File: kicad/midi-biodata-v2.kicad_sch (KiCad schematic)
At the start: 32 parts, among them J1 DIN-5_180degree, J2 PJ-320B, J3 Conn_01x14_Pin, J5 PJ-320B, J6 PJ-320B, U1 SN74LVC1G07DBVR, U3 LMC555xM

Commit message: send to jlcpcb
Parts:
- C5: value 1uF -> 100uF
- D8, D9: LCSC C85401 -> C294611
- J3: footprint Connector_PinHeader_2.54mm:PinHeader_1x12_P2.54mm_Vertical -> Connector_PinHeader_2.54mm:PinHeader_1x13_P2.54mm_Vertical
- RV1: footprint Potentiometer_THT:Potentiometer_Bourns_3296W_Vertical -> Potentiometer_THT:Potentiometer_Alps_RK09K_Single_Vertical
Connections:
- net +3V3 is gone; now on net +5V: J3.12 (Pin_12)
- net GND: now also J3.13 (Pin_13)
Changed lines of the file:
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@@
 			)
 		)
-		(property "Value" "1uF"
+		(property "Value" "100uF"
 			(at 141.224 40.386 0)
 			(effects
@@
 			)
 		)
-		(property "LCSC" "C85401"
+		(property "LCSC" "C294611"
 			(at 157.48 60.96 0)
 			(effects
@@
 			)
 		)
-		(property "LCSC" "C85401"
+		(property "LCSC" "C294611"
 			(at 168.91 40.64 0)
 			(effects
@@
 		)
 		(property "Value" "+5V"
-			(at 136.398 163.83 0)
+			(at 135.636 163.83 0)
 			(effects
 				(font
@@
 			)
 		)
-		(property "Footprint" "Connector_PinHeader_2.54mm:PinHeader_1x12_P2.54mm_Vertical"
+		(property "Footprint" "Connector_PinHeader_2.54mm:PinHeader_1x13_P2.54mm_Vertical"
 			(at 124.46 153.67 0)
 			(effects
@@
 			)
 		)
-		(property "Value" "+3V3"
-			(at 133.604 166.878 0)
+		(property "Value" "+5V"
+			(at 135.382 166.624 0)
 			(effects
 				(font
@@
 			)
 		)
-		(property "Footprint" "Potentiometer_THT:Potentiometer_Bourns_3296W_Vertical"
+		(property "Footprint" "Potentiometer_THT:Potentiometer_Alps_RK09K_Single_Vertical"
 			(at 137.16 101.6 0)
 			(effects
@@
 			)
 		)
+		(property "LCSC" ""
+			(at 137.16 101.6 0)
+			(effects
+				(font
+					(size 1.27 1.27)
+				)
+				(hide yes)
+			)
+		)
 		(pin "2"
 		)
@@
 					(unit 1)
 				)
+			)
+		)
+	)
+	(symbol
+		(lib_id "midi-biodata-v2-rescue:GND")
+		(at 129.54 168.91 90)
+		(unit 1)
+		(exclude_from_sim no)
+		(in_bom yes)
+		(on_board yes)
+		(dnp no)
+		(property "Reference" "#PWR018"
+			(at 135.89 168.91 0)
+			(effects
+				(font
+					(size 1.27 1.27)
+				)
+				(hide yes)
+			)
+		)
+		(property "Value" "GND"
+			(at 133.35 168.91 0)
+			(effects
+				(font
+					(size 1.27 1.27)
+				)
+			)
+		)
+		(property "Footprint" ""
+			(at 129.54 168.91 0)
+			(effects
+				(font
+					(size 1.27 1.27)
+				)
+				(hide yes)
+			)
+		)
+		(property "Datasheet" ""
+			(at 129.54 168.91 0)
+			(effects
+				(font
+					(size 1.27 1.27)
+				)
+				(hide yes)
+			)
+		)
+		(property "Description" ""
+			(at 129.54 168.91 0)
+			(effects
+				(font
+					(size 1.27 1.27)
+				)
+				(hide yes)
+			)
+		)
+		(pin "1"
+		)
+		(instances
+			(project "midi-biodata-v2"
+				(path "/0696d548-26ae-48fa-b73e-c6b82482150e"
+					(reference "#PWR018")
+					(unit 1)
+				)

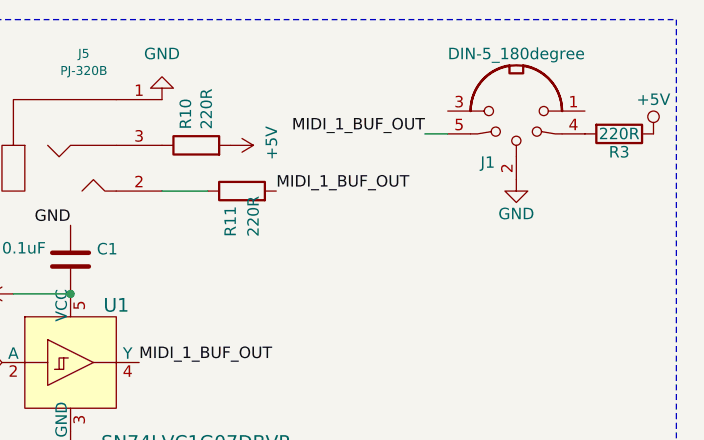
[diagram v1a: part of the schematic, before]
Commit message: fixed midi routing on the pcb board
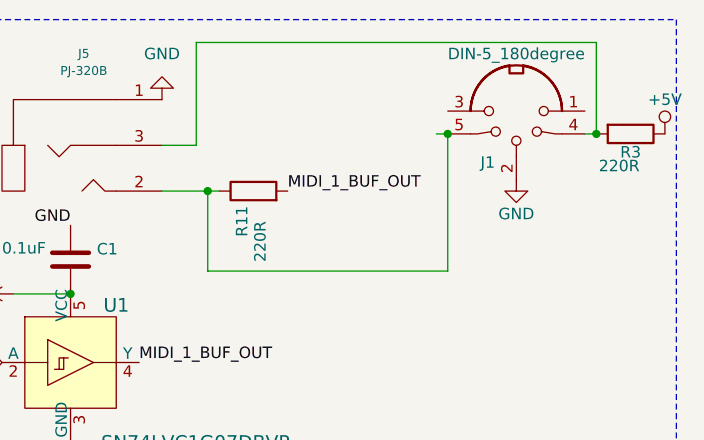
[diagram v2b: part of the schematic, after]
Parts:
- removed R10: 220R, Resistor_SMD:R_0402_1005Metric, symbol Device:R
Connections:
- net MIDI_1_BUF_OUT: no longer J1.5
- net at J1.4, R3.2: now also J5.3
- net at J5.2, R11.1: now also J1.5
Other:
- moved on the sheet: R11, R3

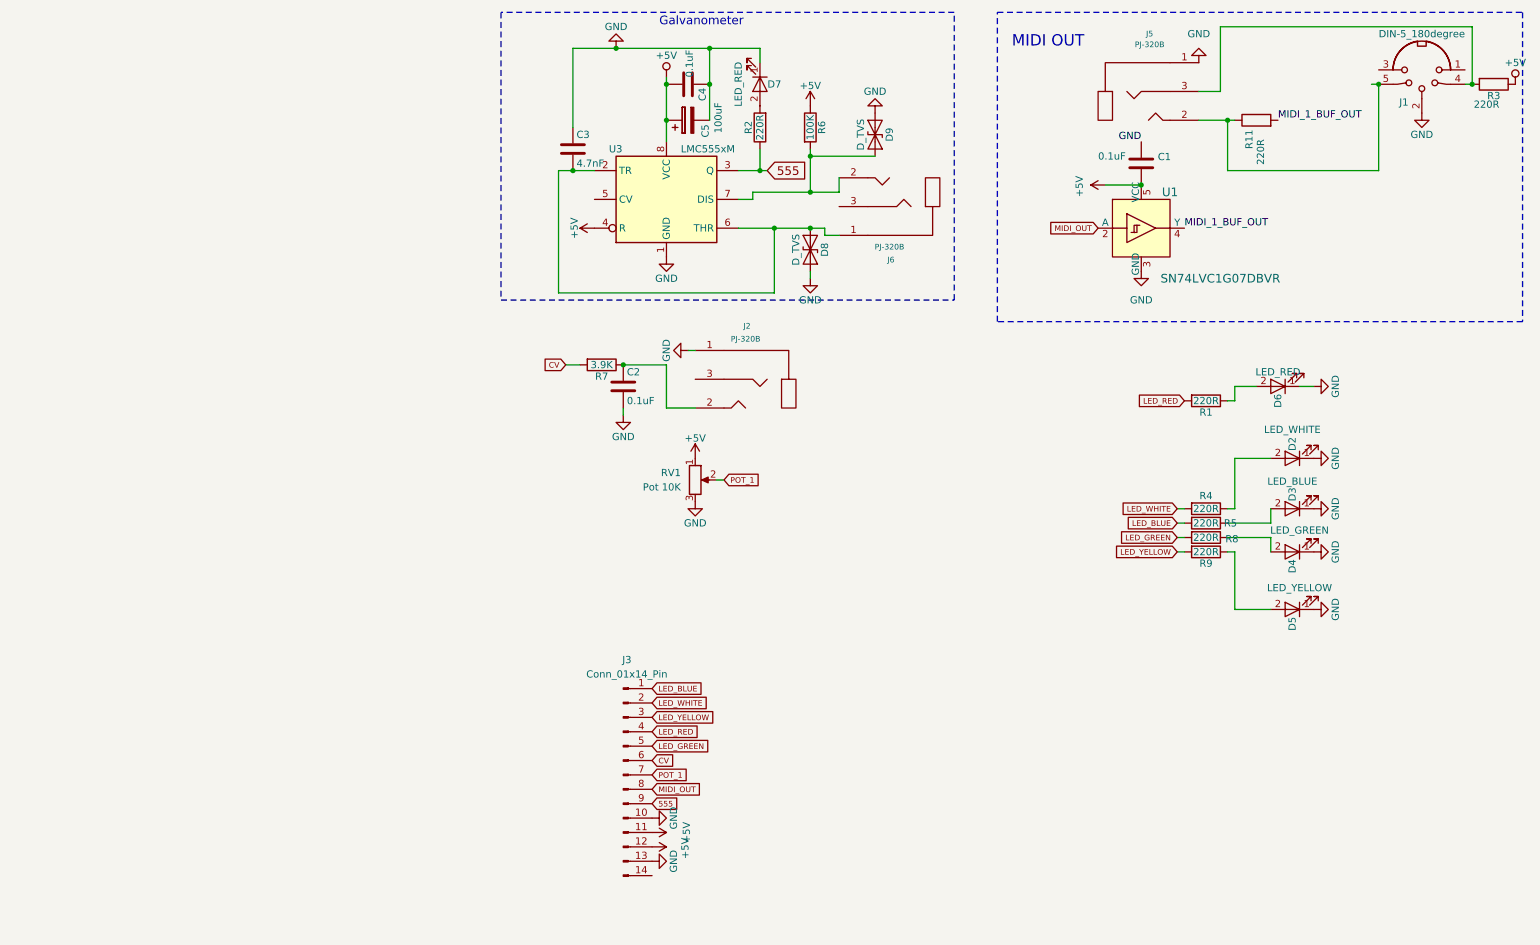
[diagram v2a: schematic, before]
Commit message: cleanup, changed footprint for 3.5mm jack
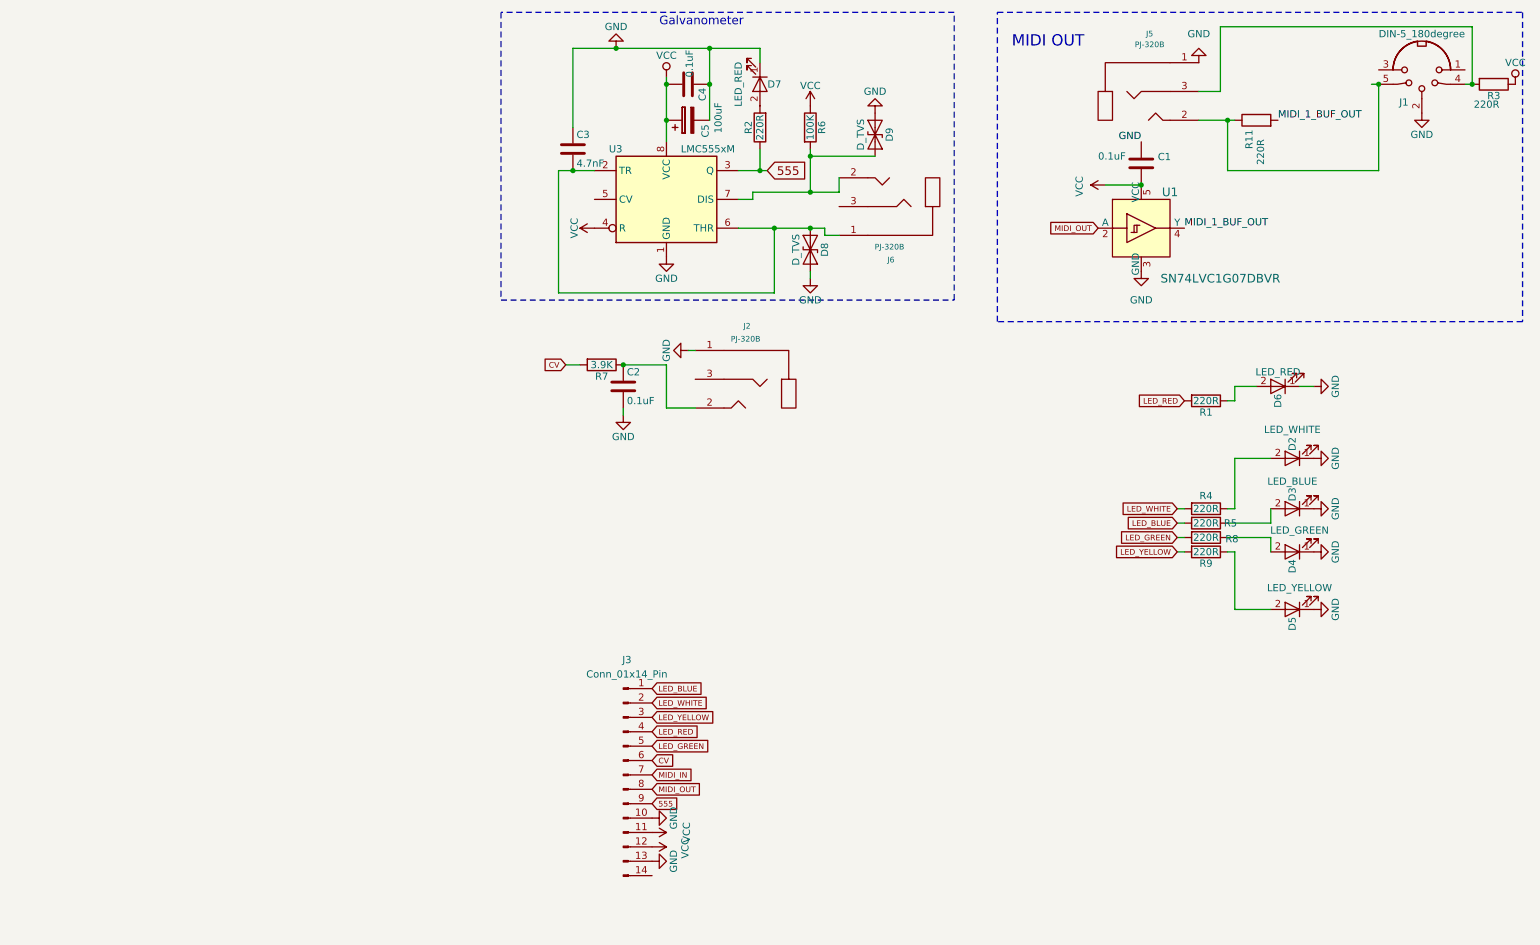
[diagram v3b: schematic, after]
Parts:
- removed RV1: Pot 10K, Potentiometer_THT:Potentiometer_Alps_RK09K_Single_Vertical, symbol Device:R_Potentiometer
- J2, J5, J6: footprint poma:3.5mm_stereo_jack_PJ320B -> poma:3.5mm_stereo_jack_PJ320B_THRU
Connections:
- net +5V renamed VCC
- net POT_1 renamed MIDI_IN

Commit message: Add esp32s2 supermini board
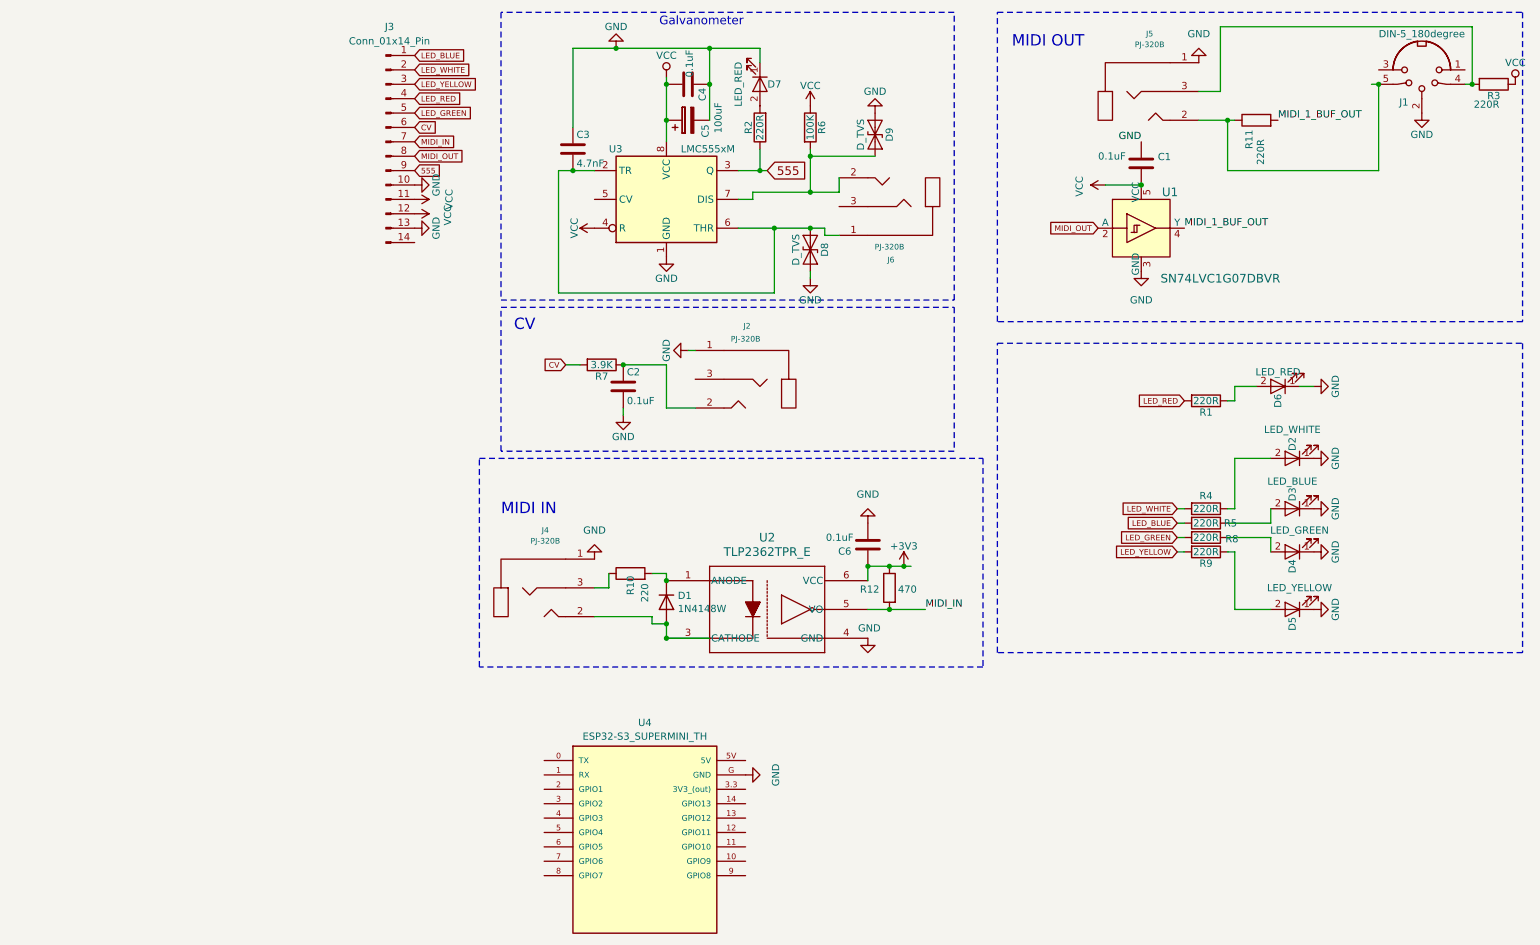
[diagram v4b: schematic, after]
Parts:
- added C6: 0.1uF, Capacitor_SMD:C_0402_1005Metric, symbol Device:C
- added D1: 1N4148W, Diode_SMD:D_SOD-123, symbol Diode:1N914
- added J4: PJ-320B, poma:3.5mm_stereo_jack_PJ320B_THRU, symbol poma:PJ-320B
- added R10: 220, Resistor_SMD:R_0402_1005Metric, symbol Device:R
- added R12: 470, Resistor_SMD:R_0603_1608Metric_Pad0.98x0.95mm_HandSolder, symbol Device:R
- added U2: TLP2362TPR_E, poma:tlp2362, symbol Sleep-lib:TLP2362TPR_E
- added U4: ESP32-S3_SUPERMINI_TH, ESP32-C3_SUPERMINI_TH:MODULE_ESP32-C3_SUPERMINI_TH, symbol esp32s3_supermini:ESP32-S3_SUPERMINI_TH
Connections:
- net GND: now also C6.2, J4.1, U2.4 (GND), U4.G (GND)
- net MIDI_IN: now also R12.2, U2.5 (VO)
- new net: J4.3, R10.1
- new net: D1.1 (K), R10.2, U2.1 (ANODE)
- new net: D1.2 (A), J4.2, U2.3 (CATHODE)
- new net +3V3: C6.1, R12.1, U2.6 (VCC)
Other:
- note added: "CV"
- note added: "MIDI IN"
- moved on the sheet: J3

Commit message: updated board with esp32 s3 mini integration
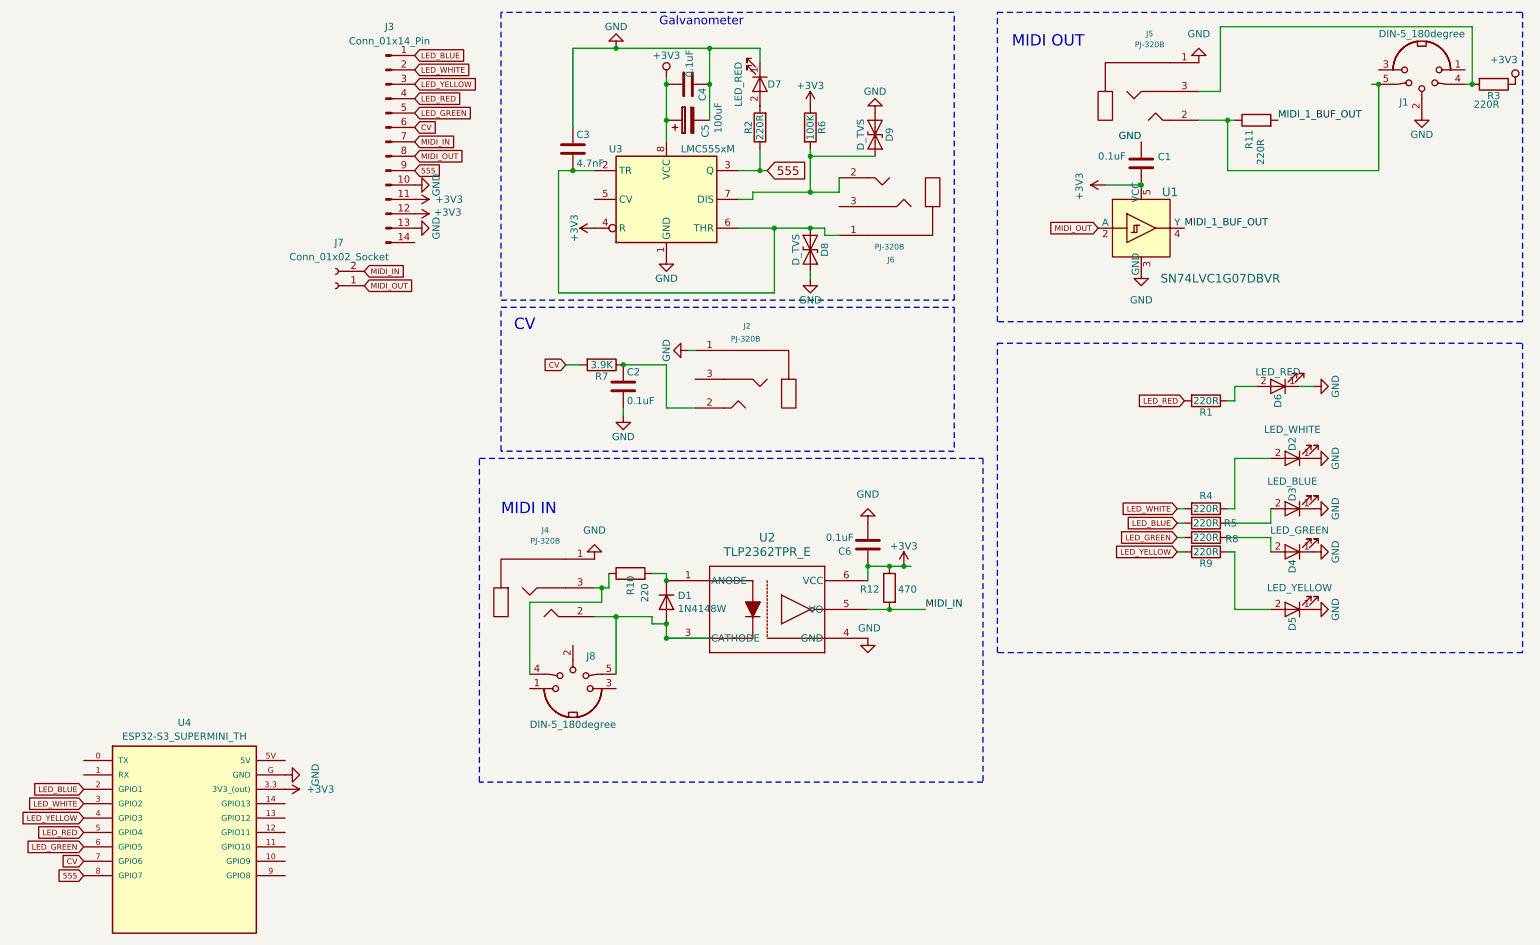
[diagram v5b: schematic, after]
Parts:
- added J7: Conn_01x02_Socket, Connector_PinHeader_2.54mm:PinHeader_1x02_P2.54mm_Vertical, symbol Connector:Conn_01x02_Socket
- added J8: DIN-5_180degree, midi-jack:DIN-5-MIDI-JACK, symbol midi-biodata-v2-rescue:DIN-5_180degree
- U4: footprint ESP32-C3_SUPERMINI_TH:MODULE_ESP32-C3_SUPERMINI_TH -> esp32s3mini:MODULE_ESP32-C3_SUPERMINI_TH
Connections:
- net VCC is gone; now on net +3V3: C1.2, C4.2, C5.1, J3.11 (Pin_11), J3.12 (Pin_12), R3.1, R6.1, U1.5 (VCC), U3.4 (R), U3.8 (VCC)
- net +3V3: now also U4.3.3 (3V3_(out))
- net 555: now also U4.8 (GPIO7)
- net CV: now also U4.7 (GPIO6)
- net LED_BLUE: now also U4.2 (GPIO1)
- net LED_GREEN: now also U4.6 (GPIO5)
- net LED_RED: now also U4.5 (GPIO4)
- net LED_WHITE: now also U4.3 (GPIO2)
- net LED_YELLOW: now also U4.4 (GPIO3)
- net MIDI_IN: now also J7.2 (Pin_2)
- net MIDI_OUT: now also J7.1 (Pin_1)
- net at J4.3, R10.1: now also J8.4
- net at D1.2 (A), J4.2, U2.3 (CATHODE): now also J8.5
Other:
- moved on the sheet: U4

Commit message: send v0.2 to production
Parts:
- R10: value 220 -> 220R
- R12: footprint Resistor_SMD:R_0603_1608Metric_Pad0.98x0.95mm_HandSolder -> Resistor_SMD:R_0805_2012Metric

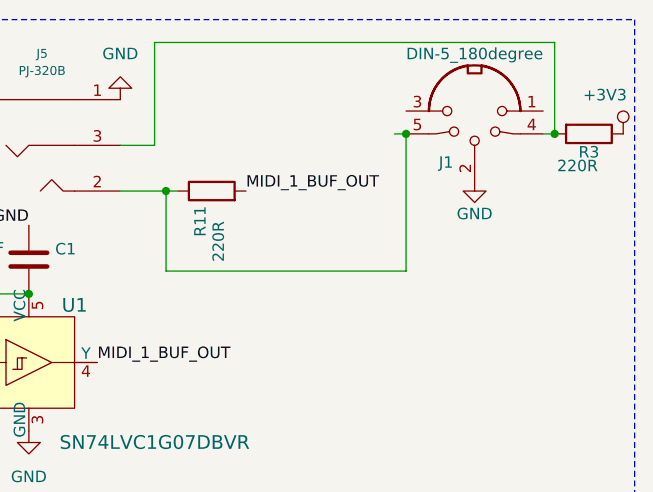
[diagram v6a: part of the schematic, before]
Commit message: Update MIDI out resistors for 3.3v
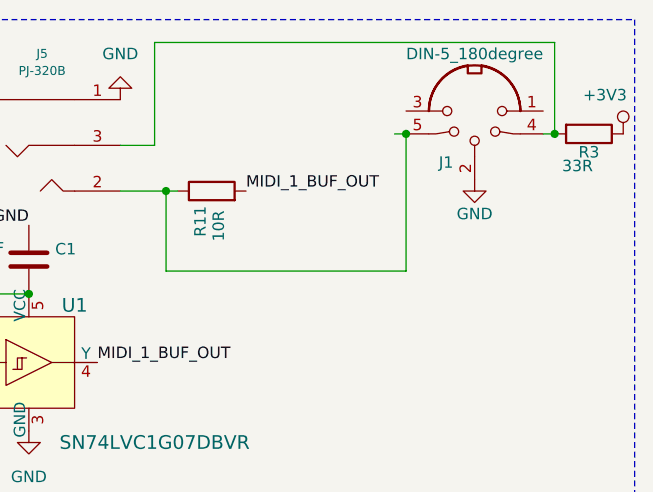
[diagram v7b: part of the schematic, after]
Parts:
- R11: value 220R -> 10R; LCSC C25091 -> C25077
- R3: value 220R -> 33R; LCSC C25091 -> C25105
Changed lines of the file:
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@@
 		(title "MIDI Biodata Sonification Device ")
 		(date "2018-01-12")
+		(rev "0.3")
 		(company "13-37.org electronics")
 	)
